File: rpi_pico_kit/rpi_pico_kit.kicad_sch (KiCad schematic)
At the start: 27 parts, among them J1 Barrel_Jack_Switch, J2 Conn_01x03_Male, Q1 BC807, Q2 BC807, SW1 SW_Push, U1 RPi Pico

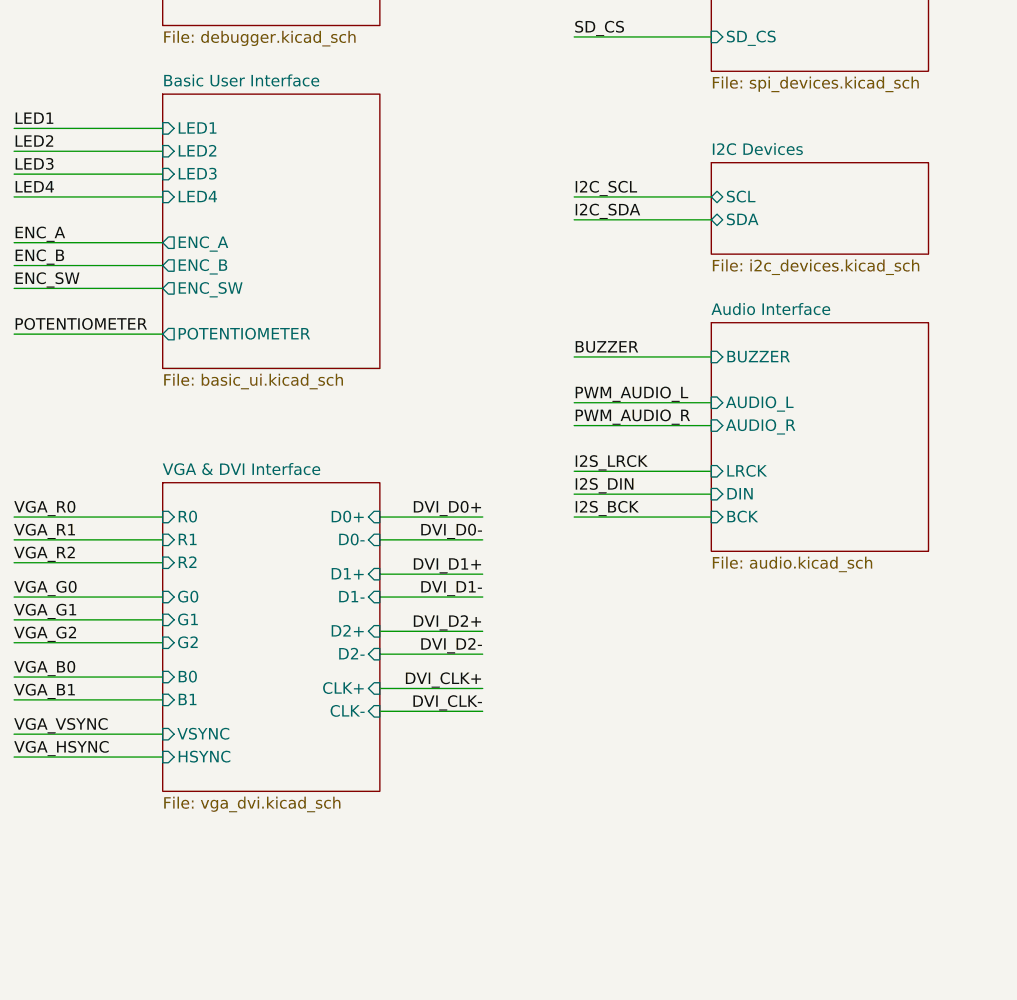
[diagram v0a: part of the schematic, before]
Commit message: added i2c interface for vga and dvi
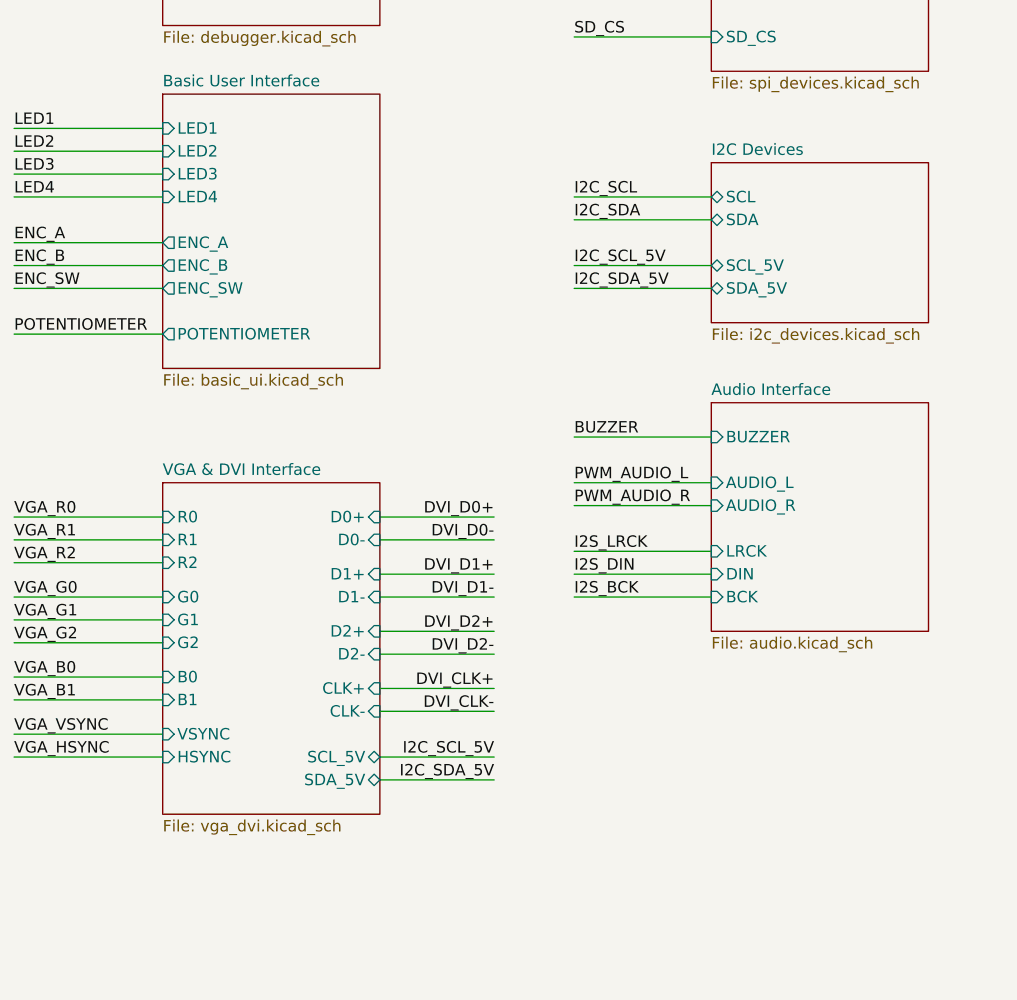
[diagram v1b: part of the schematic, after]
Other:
- sheet I2C Devices ports: added SCL_5V, SDA_5V; removed none
- sheet VGA & DVI Interface ports: added SCL_5V, SDA_5V; removed none

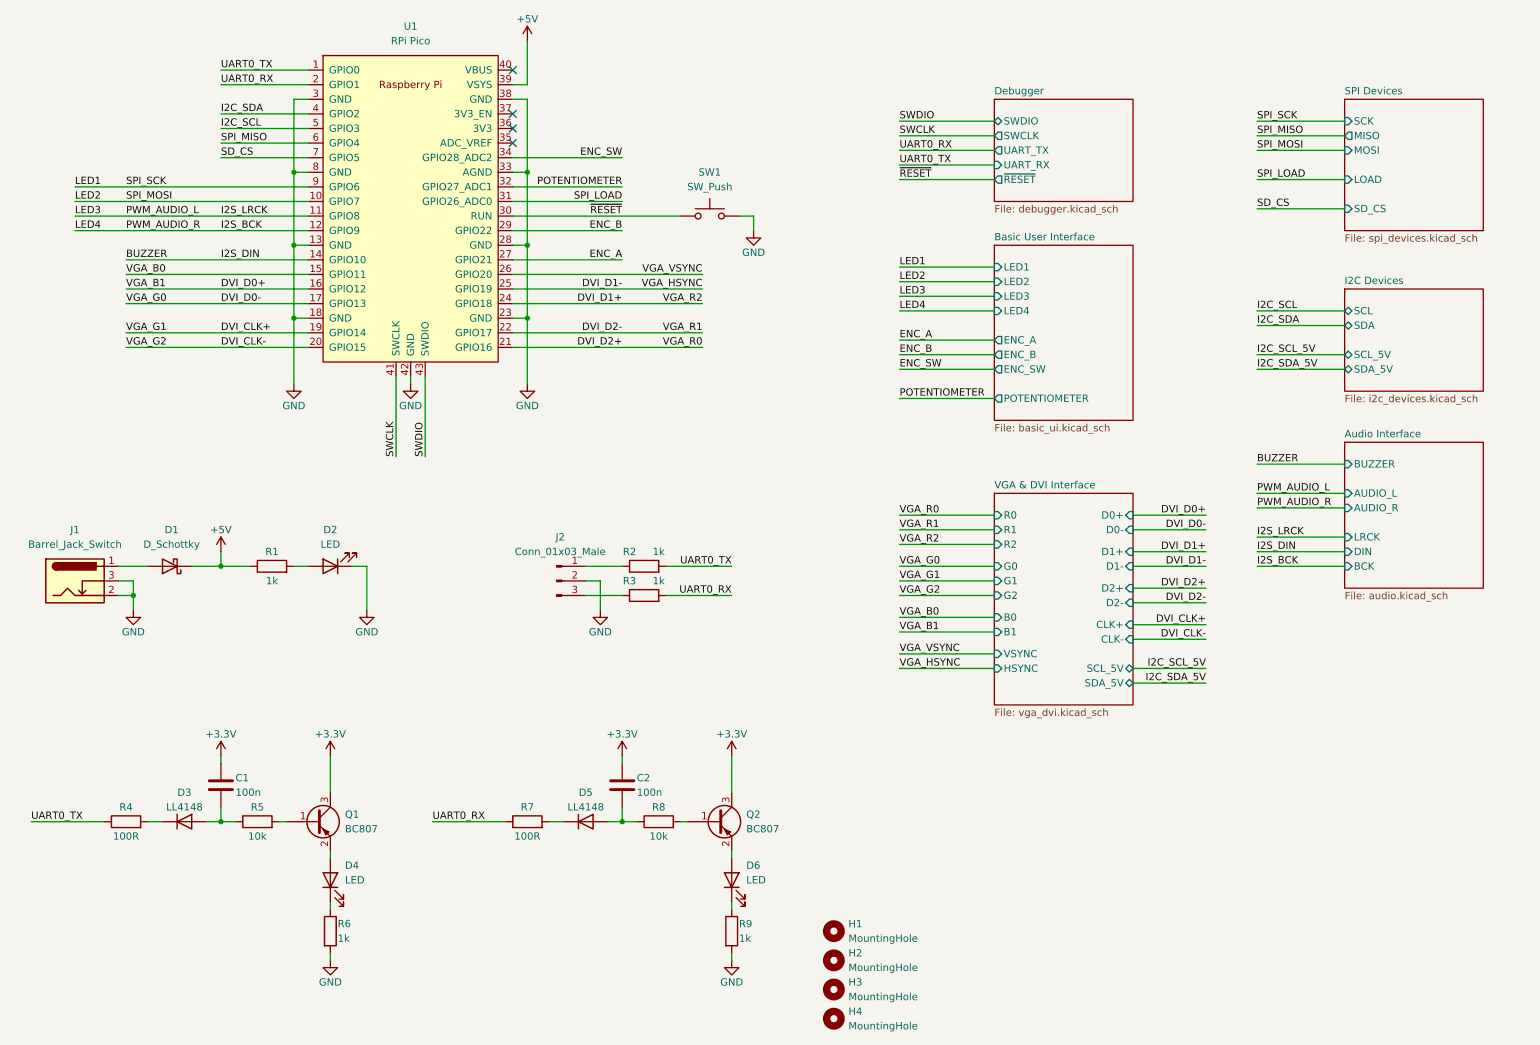
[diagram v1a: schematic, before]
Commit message: added uart selector
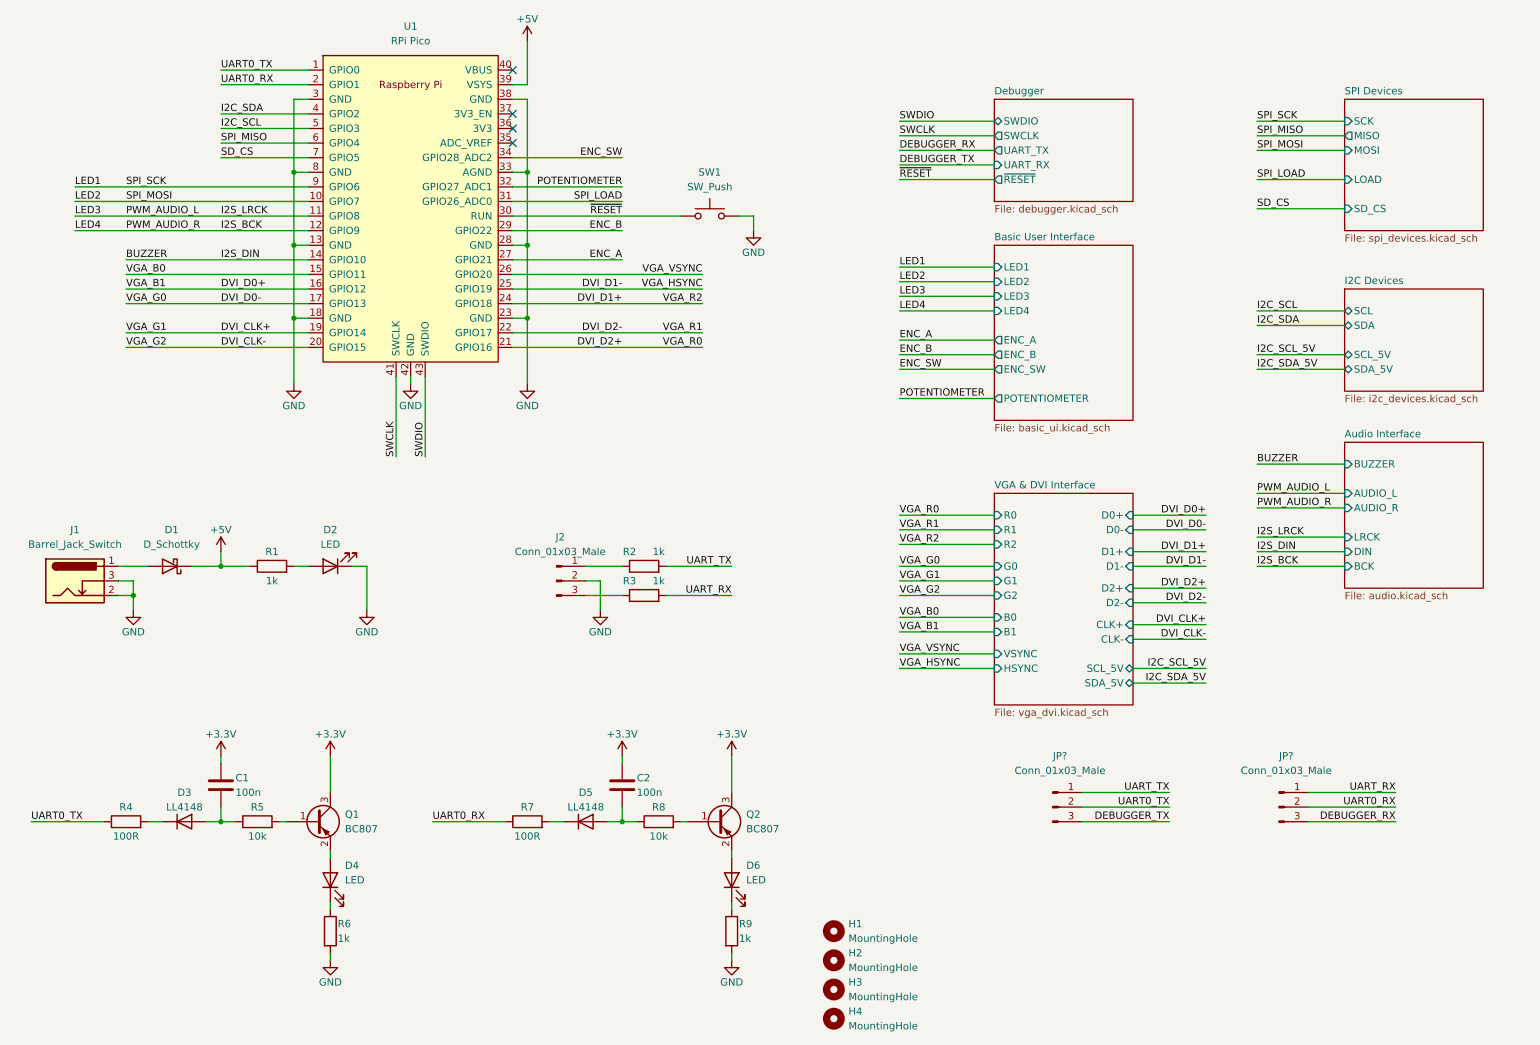
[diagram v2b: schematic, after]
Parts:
- added JP? (x2): Conn_01x03_Male, symbol Connector:Conn_01x03_Male
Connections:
- net UART0_RX: now also JP?.2 (Pin_2); no longer R3.2
- net UART0_TX: now also JP?.2 (Pin_2); no longer R2.2
- new net DEBUGGER_RX: JP?.3 (Pin_3)
- new net DEBUGGER_TX: JP?.3 (Pin_3)
- new net UART_RX: JP?.1 (Pin_1), R3.2
- new net UART_TX: JP?.1 (Pin_1), R2.2
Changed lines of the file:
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@@
+    (stroke (width 0) (type default))
+  )
+  (wire (pts (xy 203.2 157.48) (xy 218.44 157.48))
     (stroke (width 0) (type default))
   )
@@
     (stroke (width 0) (type default))
   )
+  (wire (pts (xy 203.2 154.94) (xy 218.44 154.94))
+    (stroke (width 0) (type default))
+  )
   (wire (pts (xy 78.74 115.57) (xy 78.74 123.19))
     (stroke (width 0) (type default))
@@
     (stroke (width 0) (type default))
   )
+  (wire (pts (xy 242.57 154.94) (xy 257.81 154.94))
+    (stroke (width 0) (type default))
+  )
   (wire (pts (xy 233.68 78.74) (xy 248.92 78.74))
     (stroke (width 0) (type default))
@@
     (stroke (width 0) (type default))
   )
+  (wire (pts (xy 242.57 157.48) (xy 257.81 157.48))
+    (stroke (width 0) (type default))
+  )
   (wire (pts (xy 66.04 34.29) (xy 66.04 46.99))
     (stroke (width 0) (type default))
@@
     (stroke (width 0) (type default))
   )
+  (wire (pts (xy 203.2 160.02) (xy 218.44 160.02))
+    (stroke (width 0) (type default))
+  )
   (wire (pts (xy 212.09 133.35) (xy 224.79 133.35))
     (stroke (width 0) (type default))
@@
     (stroke (width 0) (type default))
   )
+  (wire (pts (xy 242.57 160.02) (xy 257.81 160.02))
+    (stroke (width 0) (type default))
+  )
   (wire (pts (xy 171.45 81.28) (xy 187.96 81.28))
     (stroke (width 0) (type default))
@@
     (effects (font (size 1.27 1.27)) (justify left bottom))
   )
-  (label "UART0_TX" (at 171.45 45.72 0) (fields_autoplaced)
+  (label "DEBUGGER_TX" (at 171.45 45.72 0) (fields_autoplaced)
     (effects (font (size 1.27 1.27)) (justify left bottom))
   )
@@
     (effects (font (size 1.27 1.27)) (justify left bottom))
   )
+  (label "UART0_TX" (at 218.44 157.48 0) (fields_autoplaced)
+    (effects (font (size 1.27 1.27)) (justify right bottom))
+  )
   (label "I2C_SCL" (at 233.68 71.12 0) (fields_autoplaced)
     (effects (font (size 1.27 1.27)) (justify left bottom))
@@
     (effects (font (size 1.27 1.27)) (justify left bottom))
   )
-  (label "UART0_RX" (at 142.24 120.65 0) (fields_autoplaced)
+  (label "UART_RX" (at 142.24 120.65 0) (fields_autoplaced)
     (effects (font (size 1.27 1.27)) (justify right bottom))
   )
@@
     (effects (font (size 1.27 1.27)) (justify left bottom))
   )
-  (label "UART0_RX" (at 171.45 43.18 0) (fields_autoplaced)
+  (label "DEBUGGER_RX" (at 171.45 43.18 0) (fields_autoplaced)
     (effects (font (size 1.27 1.27)) (justify left bottom))
   )
@@
     (effects (font (size 1.27 1.27)) (justify left bottom))
   )
-  (label "UART0_TX" (at 142.24 115.57 0) (fields_autoplaced)
+  (label "UART_TX" (at 142.24 115.57 0) (fields_autoplaced)
     (effects (font (size 1.27 1.27)) (justify right bottom))
   )
@@
     (effects (font (size 1.27 1.27)) (justify left bottom))
   )
+  (label "UART_RX" (at 257.81 154.94 0) (fields_autoplaced)
+    (effects (font (size 1.27 1.27)) (justify right bottom))
+  )
   (label "VGA_G2" (at 36.83 77.47 0) (fields_autoplaced)
     (effects (font (size 1.27 1.27)) (justify left bottom))
@@
     (effects (font (size 1.27 1.27)) (justify right bottom))
   )
+  (label "DEBUGGER_TX" (at 218.44 160.02 0) (fields_autoplaced)
+    (effects (font (size 1.27 1.27)) (justify right bottom))
+  )
   (label "I2C_SCL_5V" (at 224.79 133.35 0) (fields_autoplaced)
     (effects (font (size 1.27 1.27)) (justify right bottom))
@@
     (effects (font (size 1.27 1.27)) (justify left bottom))
   )
+  (label "DEBUGGER_RX" (at 257.81 160.02 0) (fields_autoplaced)
+    (effects (font (size 1.27 1.27)) (justify right bottom))
+  )
   (label "SPI_MISO" (at 53.34 41.91 0) (fields_autoplaced)
     (effects (font (size 1.27 1.27)) (justify left bottom))
@@
     (effects (font (size 1.27 1.27)) (justify right bottom))
   )
+  (label "UART_TX" (at 218.44 154.94 0) (fields_autoplaced)
+    (effects (font (size 1.27 1.27)) (justify right bottom))
+  )
   (label "UART0_TX" (at 53.34 29.21 0) (fields_autoplaced)
     (effects (font (size 1.27 1.27)) (justify left bottom))
@@
   (label "SPI_MOSI" (at 233.68 43.18 0) (fields_autoplaced)
     (effects (font (size 1.27 1.27)) (justify left bottom))
+  )
+  (label "UART0_RX" (at 257.81 157.48 0) (fields_autoplaced)
+    (effects (font (size 1.27 1.27)) (justify right bottom))
   )
   (label "SPI_SCK" (at 233.68 38.1 0) (fields_autoplaced)
@@
     (pin "2")
   )
+  (symbol (lib_id "Connector:Conn_01x03_Male") (at 237.49 157.48 0) (unit 1)
+    (in_bom yes) (on_board yes)
+    (property "Reference" "JP?" (id 0) (at 238.76 148.59 0)
+      (effects (font (size 1.27 1.27)))
+    )
+    (property "Value" "Conn_01x03_Male" (id 1) (at 238.76 151.13 0)
+      (effects (font (size 1.27 1.27)))
+    )
+    (property "Footprint" "" (id 2) (at 237.49 157.48 0)
+      (effects (font (size 1.27 1.27)) hide)
+    )
+    (property "Datasheet" "~" (id 3) (at 237.49 157.48 0)
+      (effects (font (size 1.27 1.27)) hide)
+    )
+    (pin "1")
+    (pin "2")
+    (pin "3")
+  )
   (symbol (lib_id "Device:C") (at 53.34 153.67 180) (unit 1)
     (in_bom yes) (on_board yes)
@@
     (pin "1")
     (pin "2")
+  )
+  (symbol (lib_id "Connector:Conn_01x03_Male") (at 198.12 157.48 0) (unit 1)
+    (in_bom yes) (on_board yes)
+    (property "Reference" "JP?" (id 0) (at 199.39 148.59 0)
+      (effects (font (size 1.27 1.27)))
+    )
+    (property "Value" "Conn_01x03_Male" (id 1) (at 199.39 151.13 0)
+      (effects (font (size 1.27 1.27)))
+    )
+    (property "Footprint" "" (id 2) (at 198.12 157.48 0)
+      (effects (font (size 1.27 1.27)) hide)
+    )
+    (property "Datasheet" "~" (id 3) (at 198.12 157.48 0)
+      (effects (font (size 1.27 1.27)) hide)
+    )
+    (pin "1")
+    (pin "2")
+    (pin "3")
   )
   (symbol (lib_id "Device:D_Schottky") (at 44.45 115.57 180) (unit 1)
@@
       (reference "JP3") (unit 1) (value "Jumper_2_Open") (footprint "TestPoint:TestPoint_2Pads_Pitch2.54mm_Drill0.8mm")
     )
+    (path "/67656a88-3e99-417f-b639-7ef3302321d2"
+      (reference "JP?") (unit 1) (value "Conn_01x03_Male") (footprint "")
+    )
+    (path "/6eecff7e-30f9-4f28-984d-38395d6865ec"
+      (reference "JP?") (unit 1) (value "Conn_01x03_Male") (footprint "")
+    )
     (path "/91c22ee0-3402-49cb-8c0d-c5afcfd276c7"

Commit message: added some footprints
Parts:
- J2: footprint (none) -> Connector_PinHeader_2.54mm:PinHeader_1x03_P2.54mm_Vertical
- JP4, JP5: renamed from JP?; footprint (none) -> Connector_PinHeader_2.54mm:PinHeader_1x03_P2.54mm_Vertical
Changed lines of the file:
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@@
   (symbol (lib_id "Connector:Conn_01x03_Male") (at 237.49 157.48 0) (unit 1)
     (in_bom yes) (on_board yes)
-    (property "Reference" "JP?" (id 0) (at 238.76 148.59 0)
+    (property "Reference" "JP5" (id 0) (at 238.76 148.59 0)
       (effects (font (size 1.27 1.27)))
     )
@@
       (effects (font (size 1.27 1.27)))
     )
-    (property "Footprint" "" (id 2) (at 237.49 157.48 0)
+    (property "Footprint" "Connector_PinHeader_2.54mm:PinHeader_1x03_P2.54mm_Vertical" (id 2) (at 237.49 157.48 0)
       (effects (font (size 1.27 1.27)) hide)
     )
@@
   (symbol (lib_id "Connector:Conn_01x03_Male") (at 198.12 157.48 0) (unit 1)
     (in_bom yes) (on_board yes)
-    (property "Reference" "JP?" (id 0) (at 199.39 148.59 0)
+    (property "Reference" "JP4" (id 0) (at 199.39 148.59 0)
       (effects (font (size 1.27 1.27)))
     )
@@
       (effects (font (size 1.27 1.27)))
     )
-    (property "Footprint" "" (id 2) (at 198.12 157.48 0)
+    (property "Footprint" "Connector_PinHeader_2.54mm:PinHeader_1x03_P2.54mm_Vertical" (id 2) (at 198.12 157.48 0)
       (effects (font (size 1.27 1.27)) hide)
     )
@@
       (effects (font (size 1.27 1.27)))
     )
-    (property "Footprint" "" (id 2) (at 111.76 118.11 0)
+    (property "Footprint" "Connector_PinHeader_2.54mm:PinHeader_1x03_P2.54mm_Vertical" (id 2) (at 111.76 118.11 0)
       (effects (font (size 1.27 1.27)) hide)
     )
@@
     )
     (path "/9fa08ac3-227f-4cf0-bd88-360446d7d584/6429a062-d753-4165-91f8-badf014add71"
-      (reference "#PWR?") (unit 1) (value "GND") (footprint "")
+      (reference "#PWR0146") (unit 1) (value "GND") (footprint "")
     )
     (path "/9fa08ac3-227f-4cf0-bd88-360446d7d584/a9382fcb-fc51-4b98-bf97-972b46fc0949"
-      (reference "#PWR?") (unit 1) (value "+5V") (footprint "")
+      (reference "#PWR0147") (unit 1) (value "+5V") (footprint "")
     )
     (path "/2bd19bd1-2975-4b91-a884-8b1113539e97/a927f1f4-98ba-40b8-bb8d-0eaab95070e5"
@@
     )
     (path "/9fa08ac3-227f-4cf0-bd88-360446d7d584/6c464c76-0603-4471-9260-a10f77de9af3"
-      (reference "C?") (unit 1) (value "100n") (footprint "Capacitor_SMD:C_0805_2012Metric_Pad1.18x1.45mm_HandSolder")
+      (reference "C43") (unit 1) (value "100n") (footprint "Capacitor_SMD:C_0805_2012Metric_Pad1.18x1.45mm_HandSolder")
     )
     (path "/7347ff23-167b-4742-8802-80fd4b05fc44"
@@
     )
     (path "/ddd6a23d-057a-44b2-bd8d-c0bba27bdf0d"
-      (reference "J2") (unit 1) (value "Conn_01x03_Male") (footprint "")
+      (reference "J2") (unit 1) (value "Conn_01x03_Male") (footprint "Connector_PinHeader_2.54mm:PinHeader_1x03_P2.54mm_Vertical")
     )
     (path "/fe15dc26-52fc-427e-8179-2b8bb41b57bb/b746b086-d024-409d-bd6c-0149ccf84dd5"
@@
       (reference "JP3") (unit 1) (value "Jumper_2_Open") (footprint "TestPoint:TestPoint_2Pads_Pitch2.54mm_Drill0.8mm")
     )
+    (path "/6eecff7e-30f9-4f28-984d-38395d6865ec"
+      (reference "JP4") (unit 1) (value "Conn_01x03_Male") (footprint "Connector_PinHeader_2.54mm:PinHeader_1x03_P2.54mm_Vertical")
+    )
     (path "/67656a88-3e99-417f-b639-7ef3302321d2"
-      (reference "JP?") (unit 1) (value "Conn_01x03_Male") (footprint "")
-    )
-    (path "/6eecff7e-30f9-4f28-984d-38395d6865ec"
-      (reference "JP?") (unit 1) (value "Conn_01x03_Male") (footprint "")
+      (reference "JP5") (unit 1) (value "Conn_01x03_Male") (footprint "Connector_PinHeader_2.54mm:PinHeader_1x03_P2.54mm_Vertical")
     )
     (path "/91c22ee0-3402-49cb-8c0d-c5afcfd276c7"
